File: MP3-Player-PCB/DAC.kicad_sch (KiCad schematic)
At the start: 16 parts, among them U401 TAD5242, U402 ST-0322D00-071-1A2H, U403 TPD4E1U06

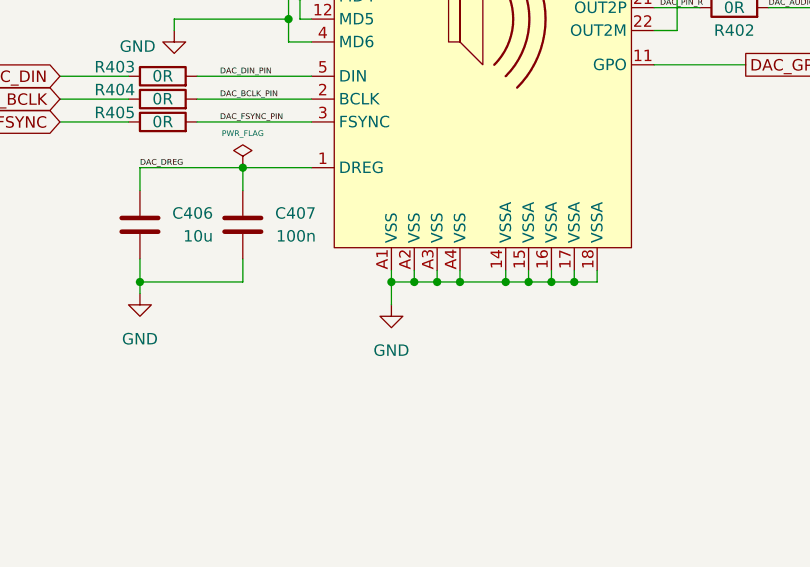
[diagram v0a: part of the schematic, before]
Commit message: Fixed all import change from schematic errors and warnings
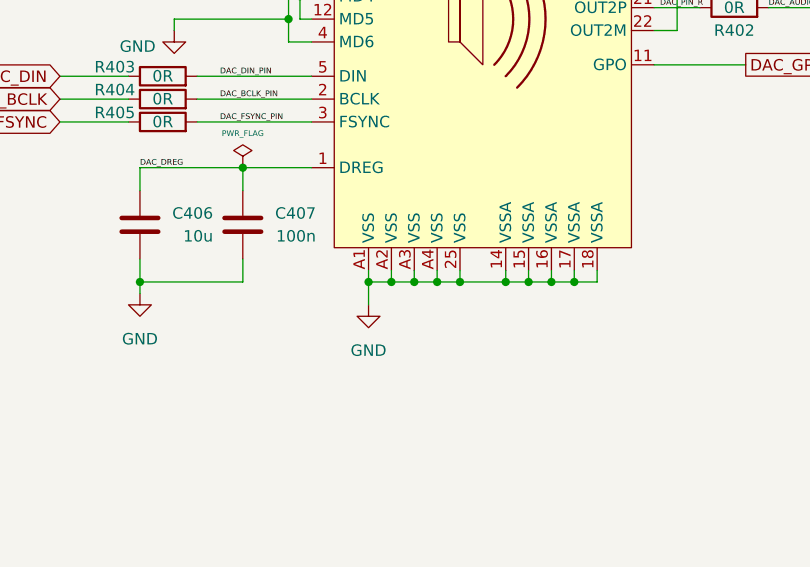
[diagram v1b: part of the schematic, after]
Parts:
- U401: footprint Package_DFN_QFN:VQFN-24-1EP_4x4mm_P0.5mm_EP2.5x2.5mm -> MP3-Player_Footprint_Libraries:TAD5242
- U403: footprint Package_TO_SOT_SMD:SOT-23-5 -> Package_TO_SOT_SMD:SOT-23-6
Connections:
- net GND: now also U401.25 (VSS)
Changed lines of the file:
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@@
+	)
+	(junction
+		(at 99.06 128.27)
+		(diameter 0)
+		(color 0 0 0 0)
 	)
 	(junction
@@
 	(wire
 		(pts
+			(xy 99.06 127) (xy 99.06 128.27)
+		)
+		(stroke
+			(width 0)
+			(type default)
+		)
+	)
+	(wire
+		(pts
 			(xy 95.25 55.88) (xy 83.82 55.88)
 		)
@@
 	(wire
 		(pts
-			(xy 101.6 128.27) (xy 101.6 130.81)
+			(xy 99.06 128.27) (xy 99.06 130.81)
+		)
+		(stroke
+			(width 0)
+			(type default)
+		)
+	)
+	(wire
+		(pts
+			(xy 99.06 128.27) (xy 101.6 128.27)
 		)
 		(stroke
@@
 			)
 		)
-		(property "Footprint" "Package_TO_SOT_SMD:SOT-23-5"
+		(property "Footprint" "Package_TO_SOT_SMD:SOT-23-6"
 			(at 210.82 135.89 0)
 			(effects
@@
 	(symbol
 		(lib_id "power:GND")
-		(at 101.6 130.81 0)
+		(at 99.06 130.81 0)
 		(unit 1)
 		(exclude_from_sim no)
@@
 		(fields_autoplaced yes)
 		(property "Reference" "#PWR0412"
-			(at 101.6 137.16 0)
+			(at 99.06 137.16 0)
 			(effects
 				(font
@@
 		)
 		(property "Value" "GND"
-			(at 101.6 135.89 0)
+			(at 99.06 135.89 0)
 			(effects
 				(font
@@
 		)
 		(property "Footprint" ""
-			(at 101.6 130.81 0)
+			(at 99.06 130.81 0)
 			(effects
 				(font
@@
 		)
 		(property "Datasheet" ""
-			(at 101.6 130.81 0)
+			(at 99.06 130.81 0)
 			(effects
 				(font
@@
 		)
 		(property "Description" "Power symbol creates a global label with name \"GND\" , ground"
-			(at 101.6 130.81 0)
+			(at 99.06 130.81 0)
 			(effects
 				(font
@@
 			)
 		)
-		(property "Footprint" "Package_DFN_QFN:VQFN-24-1EP_4x4mm_P0.5mm_EP2.5x2.5mm"
+		(property "Footprint" "MP3-Player_Footprint_Libraries:TAD5242"
 			(at 111.76 76.2 0)
 			(effects
@@
 		(pin "17"
 		)
+		(pin "25"
+		)
 		(instances

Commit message: Much better initial layout
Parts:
- removed R403, R404, R405: 0R, Resistor_SMD:R_0603_1608Metric, symbol Device:R
- C401, C404, C405, C406: footprint Capacitor_SMD:C_0805_2012Metric -> Capacitor_SMD:C_0603_1608Metric
- C402, C403, C407: footprint Capacitor_SMD:C_0603_1608Metric -> Capacitor_SMD:C_0402_1005Metric
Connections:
- net DAC_BCLK_PIN is gone; now on net DAC_BCLK: U401.2 (BCLK)
- net DAC_DIN_PIN is gone; now on net DAC_DIN: U401.5 (DIN)
- net DAC_FSYNC_PIN is gone; now on net DAC_FSYNC: U401.3 (FSYNC)

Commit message: Routed out shipping mode exit logic circuitry
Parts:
- R401, R402: footprint Resistor_SMD:R_0603_1608Metric -> Resistor_SMD:R_0402_1005Metric
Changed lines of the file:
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@@
 			)
 		)
-		(property "Footprint" "Resistor_SMD:R_0603_1608Metric"
+		(property "Footprint" "Resistor_SMD:R_0402_1005Metric"
 			(at 139.7 94.488 90)
 			(effects
@@
 			)
 		)
-		(property "Footprint" "Resistor_SMD:R_0603_1608Metric"
+		(property "Footprint" "Resistor_SMD:R_0402_1005Metric"
 			(at 139.7 99.568 90)
 			(effects

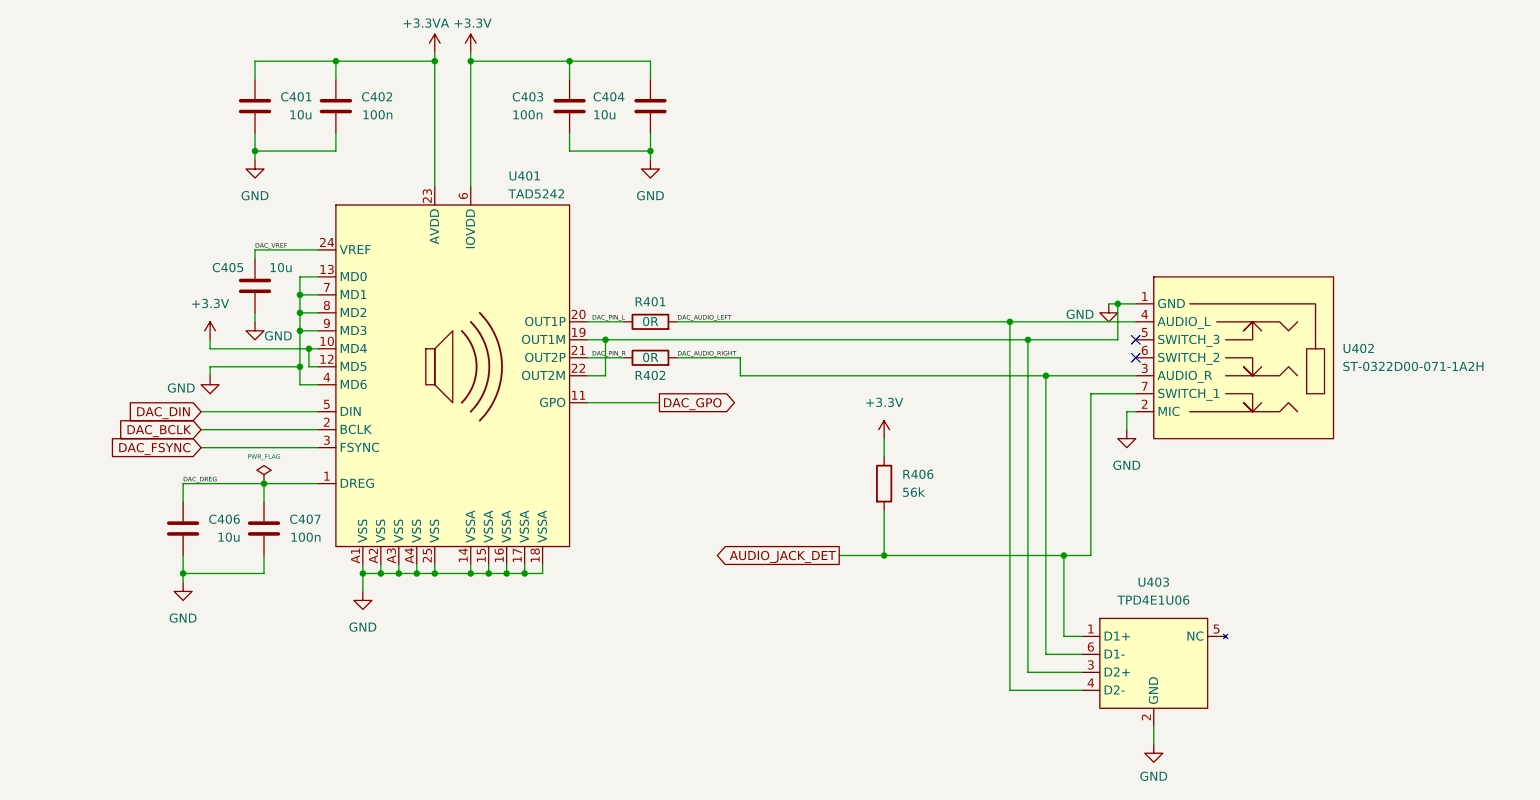
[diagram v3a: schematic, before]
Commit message: Finished Audio Jack routing
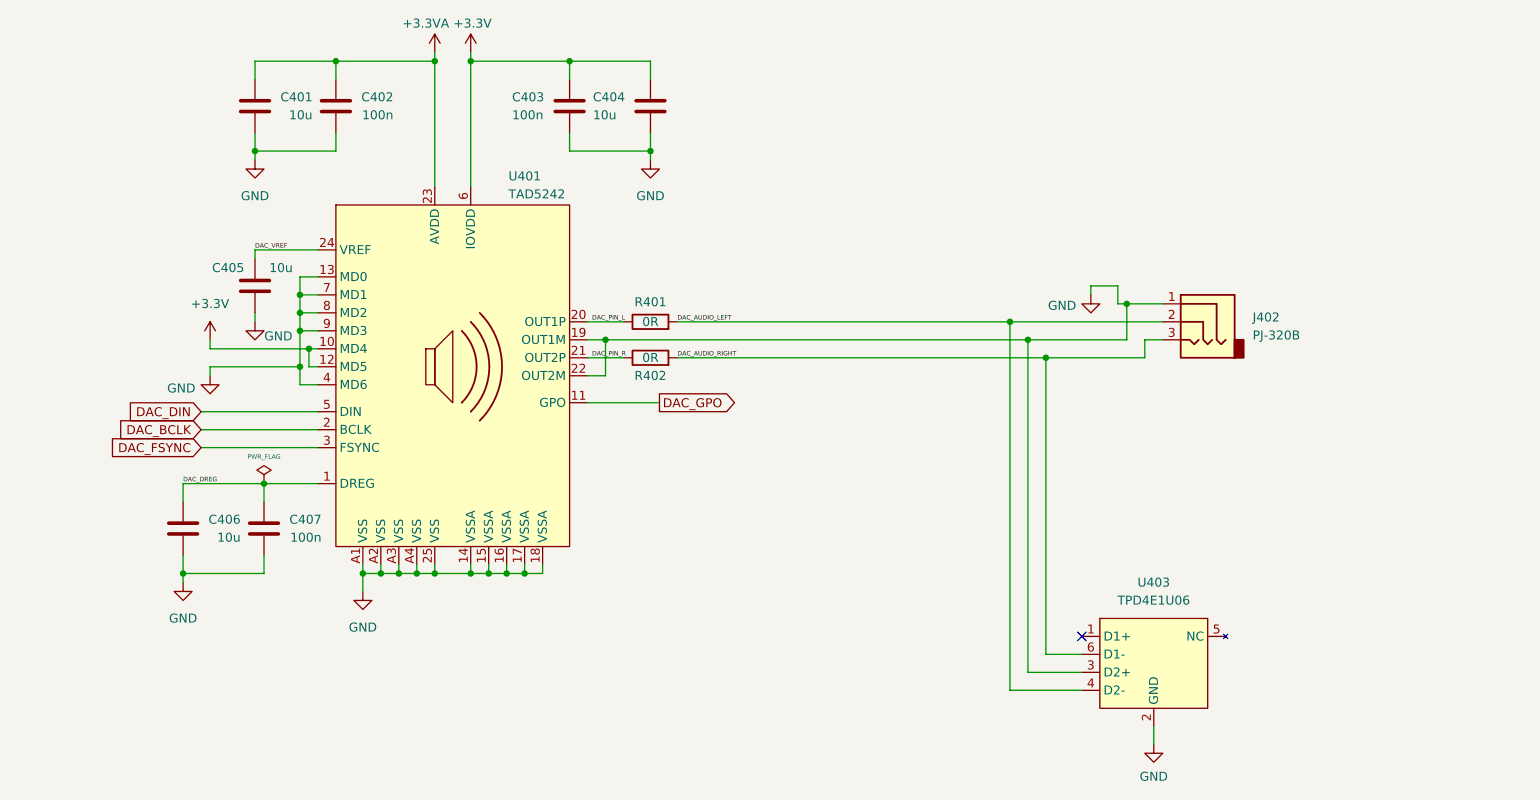
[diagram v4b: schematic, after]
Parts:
- removed R406: 56k, Resistor_SMD:R_0402_1005Metric, symbol Device:R
- removed U402: ST-0322D00-071-1A2H, MP3-Player_Footprint_Libraries:ST-0322D00-071-1A2H, symbol MP3-Player_Symbol_Libraries:ST-0322D00-071-1A2H
- added J402: PJ-320B, MP3-Player_Footprint_Libraries:PJ-320B, symbol Connector_Audio:AudioJack3
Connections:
- net DAC_AUDIO_LEFT: now also J402.2
- net DAC_AUDIO_RIGHT: now also J402.3
- net GND: now also J402.1
- net AUDIO_JACK_DET: no longer names the net of U403.1 (D1+)
- no-connect marks 2 -> 1

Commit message: Assigning JLCPCB part #'s
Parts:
- C401, C404, C405, C406: JLCPCB Part # (none) -> C19702
- C402, C403, C407: JLCPCB Part # (none) -> C1525
- J402: JLCPCB Part # (none) -> C18594
- R401, R402: JLCPCB Part # (none) -> C17168
- U401: JLCPCB Part # (none) -> C42414591
- U403: JLCPCB Part # (none) -> C124691
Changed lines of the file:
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@@
+			)
+		)
+		(property "JLCPCB Part #" "C1525"
+			(at 85.09 121.92 0)
+			(effects
+				(font
+					(size 1.27 1.27)
+				)
+				(hide yes)
 			)
 		)
@@
 			)
 		)
+		(property "JLCPCB Part #" "C124691"
+			(at 210.82 135.89 0)
+			(effects
+				(font
+					(size 1.27 1.27)
+				)
+				(hide yes)
+			)
+		)
 		(pin "5"
 		)
@@
 			)
 		)
+		(property "JLCPCB Part #" "C19702"
+			(at 73.66 121.92 0)
+			(effects
+				(font
+					(size 1.27 1.27)
+				)
+				(hide yes)
+			)
+		)
 		(pin "2"
 		)
@@
 			)
 		)
+		(property "JLCPCB Part #" "C19702"
+			(at 139.7 62.23 0)
+			(effects
+				(font
+					(size 1.27 1.27)
+				)
+				(hide yes)
+			)
+		)
 		(pin "2"
 		)
@@
 			)
 		)
+		(property "JLCPCB Part #" "C1525"
+			(at 128.27 62.23 0)
+			(effects
+				(font
+					(size 1.27 1.27)
+				)
+				(hide yes)
+			)
+		)
 		(pin "2"
 		)
@@
 			)
 		)
+		(property "JLCPCB Part #" "C42414591"
+			(at 111.76 76.2 0)
+			(effects
+				(font
+					(size 1.27 1.27)
+				)
+				(hide yes)
+			)
+		)
 		(pin "16"
 		)
@@
 			)
 		)
+		(property "JLCPCB Part #" "C18594"
+			(at 217.17 92.71 0)
+			(effects
+				(font
+					(size 1.27 1.27)
+				)
+				(hide yes)
+			)
+		)
 		(pin "3"
 		)
@@
 			)
 		)
+		(property "JLCPCB Part #" "C17168"
+			(at 139.7 92.71 90)
+			(effects
+				(font
+					(size 1.27 1.27)
+				)
+				(hide yes)
+			)
+		)
 		(pin "1"
 		)
@@
 		(property "Description" "Resistor"
 			(at 139.7 97.79 0)
+			(effects
+				(font
+					(size 1.27 1.27)
+				)
+				(hide yes)
+			)
+		)
+		(property "JLCPCB Part #" "C17168"
+			(at 139.7 97.79 90)
 			(effects
 				(font
@@
 			)
 		)
+		(property "JLCPCB Part #" "C1525"
+			(at 95.25 62.23 0)
+			(effects
+				(font
+					(size 1.27 1.27)
+				)
+				(hide yes)
+			)
+		)
 		(pin "2"
 		)
@@
 			)
 		)
+		(property "JLCPCB Part #" "C19702"
+			(at 83.82 87.63 0)
+			(effects
+				(font
+					(size 1.27 1.27)
+				)
+				(hide yes)
+			)
+		)
 		(pin "2"
 		)
@@
 			(at 83.82 62.23 0)
 			(effects
+				(font
+					(size 1.27 1.27)
+				)
+				(hide yes)
+			)
+		)
+		(property "JLCPCB Part #" "C19702"
+			(at 83.82 62.23 0)
+			(effects

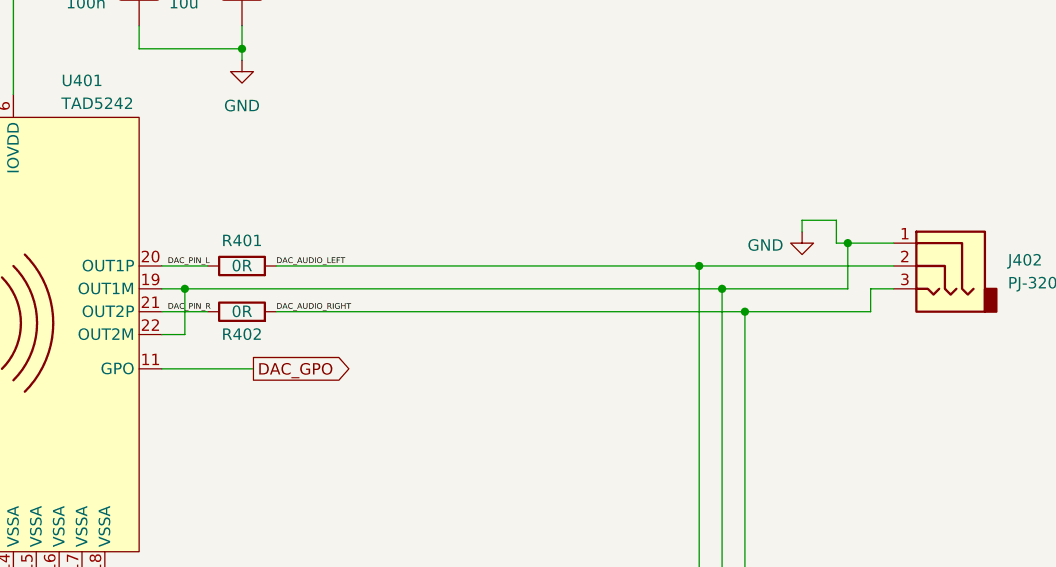
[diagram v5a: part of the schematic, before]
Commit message: Fixing common mode sense node on audio output
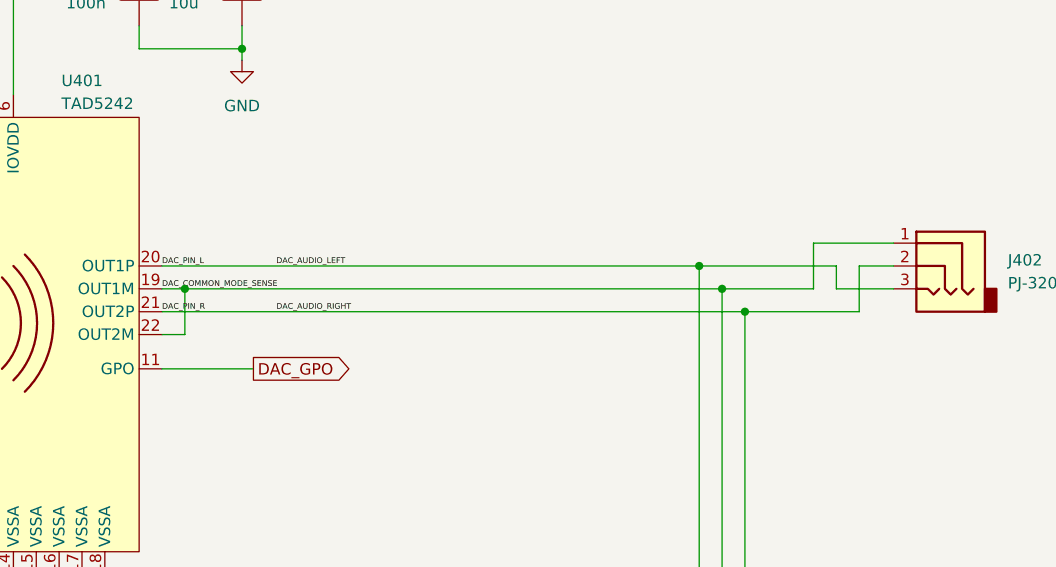
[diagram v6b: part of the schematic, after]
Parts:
- removed R401, R402: 0R, Resistor_SMD:R_0402_1005Metric, symbol Device:R
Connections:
- net DAC_PIN_L is gone; now on net DAC_AUDIO_LEFT: U401.20 (OUT1P)
- net DAC_PIN_R is gone; now on net DAC_AUDIO_RIGHT: U401.21 (OUT2P)
- net DAC_AUDIO_LEFT: now also J402.3; no longer J402.2
- net DAC_AUDIO_RIGHT: now also J402.2; no longer J402.3
- net GND: no longer J402.1, U401.19 (OUT1M), U401.22 (OUT2M), U403.3 (D2+)
- new net DAC_COMMON_MODE_SENSE: J402.1, U401.19 (OUT1M), U401.22 (OUT2M), U403.3 (D2+)
